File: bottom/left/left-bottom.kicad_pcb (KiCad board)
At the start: 2 copper layers, 137.8 x 95 mm, 8 parts

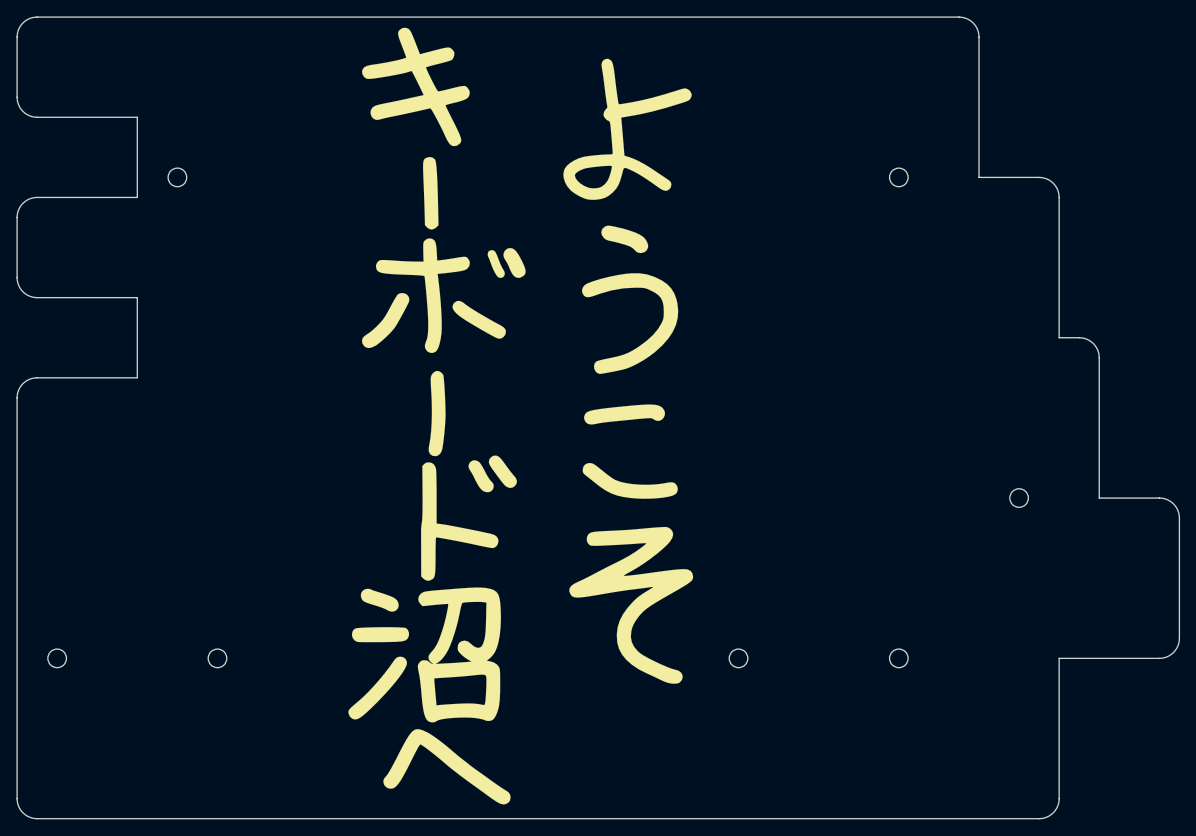
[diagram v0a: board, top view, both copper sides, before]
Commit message: shlink cutout
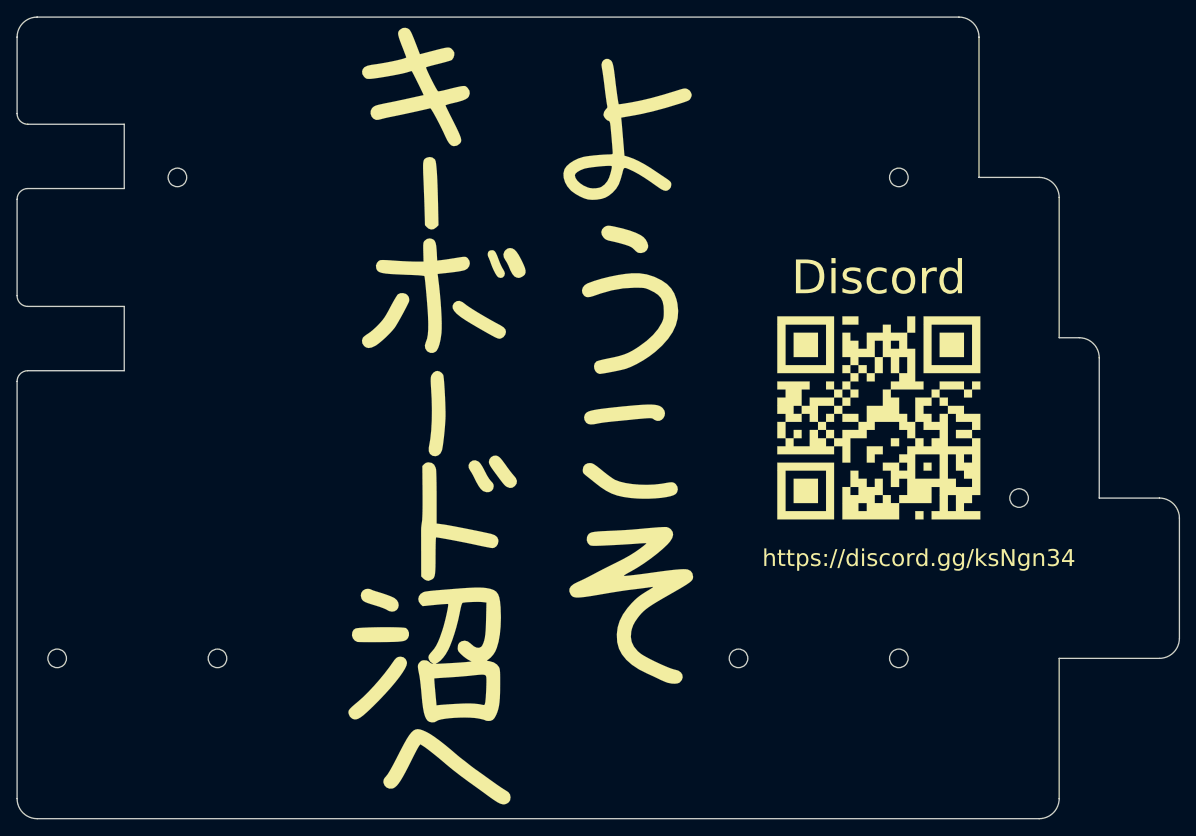
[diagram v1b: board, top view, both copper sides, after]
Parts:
- added G***: LOGO, lib:Discord_invite, F.Cu at (182.9, 104.5)
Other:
- outline, holes or cut-outs redrawn
- board text added: "Discord"
- board text added: "https://discord.gg/ksNgn34"

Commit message: move screw holl
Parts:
- moved ? 19.0 mm to (123.5, 133.0)
- moved ? 0.97 mm to (84.5, 133.0)
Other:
- board text added: "Satsuma JP SMD bottom plate rev.1"
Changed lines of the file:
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@@
   (general
     (thickness 1.6)
-    (drawings 36)
+    (drawings 37)
     (tracks 0)
     (zones 0)
@@
   )
   (module lib:MountingHole_2.2mm_M2 locked (layer F.Cu)
-    (at 104.5 133)
+    (at 123.475 133)
     (descr "Mounting Hole 2.2mm, no annular, M2")
     (tags "mounting hole 2.2mm no annular m2")
@@
   )
   (module lib:MountingHole_2.2mm_M2 locked (layer F.Cu)
-    (at 85.5 133)
+    (at 84.535 133)
     (descr "Mounting Hole 2.2mm, no annular, M2")
     (tags "mounting hole 2.2mm no annular m2")
@@
     (pad 1 np_thru_hole circle (at 0 0) (size 2.2 2.2) (drill 2.2) (layers *.Cu *.Mask))
   )
+  (gr_text "Satsuma JP SMD bottom plate rev.1" (at 179.175 147.17) (layer F.SilkS)
+    (effects (font (size 1.5 1.5) (thickness 0.3)))
+  )
   (gr_arc (start 82.02 100.18) (end 82.02 98.91) (angle -90) (layer Edge.Cuts) (width 0.05))
